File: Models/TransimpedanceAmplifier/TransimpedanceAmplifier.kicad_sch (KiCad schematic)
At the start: 2 parts, among them SW1 SW_SPDT, SW2 SW_SPDT_312

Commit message: Refactoring in progress
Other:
- note added: "Legend for bypass capacitors 0603 case size: 100 nF - 100 V, X7R 220 nF - 50 V, X7R 1 uF - 50 V, X5R 0805 case size: 1 uF - 50 V, X7R 10 uF - 25 V, X5R"
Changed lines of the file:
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@@
 	(generator_version "9.0")
 	(paper "A4")
+	(rectangle
+		(start 226.06 124.46)
+		(end 266.7 157.48)
+		(stroke
+			(width 0)
+			(type default)
+		)
+		(fill
+			(type none)
+		)
+	)
+	(text "Legend for bypass capacitors\n\n0603 case size:\n100 nF - 100 V, X7R\n220 nF - 50 V, X7R\n1 uF - 50 V, X5R\n\n0805 case size:\n1 uF - 50 V, X7R\n10 uF - 25 V, X5R"
+		(exclude_from_sim no)
+		(at 231.902 129.54 0)
+		(effects
+			(font
+				(size 1.27 1.27)
+			)
+			(justify left top)
+		)
+	)
 	(text "TODO: Limit current of bias voltage supply\nto <5 mA to prevent damage to AD8615"
 		(exclude_from_sim no)

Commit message: Save progress
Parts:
- removed SW2: SW_SPDT_312, symbol Switch:SW_SPDT_312
- added J2: Conn_01x03_Pin, symbol Connector:Conn_01x03_Pin
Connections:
- net CPU/ADC_Input: now also J2.2 (Pin_2)
- net TIA_OneStage/Output: now also J2.1 (Pin_1)
- net TIA_TwoStage/Output: now also J2.3 (Pin_3)
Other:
- note added: "Jumper selects which TIA to test Alternatively, connect DAC output directly to pin 2"
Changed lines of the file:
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@@
+		)
+	)
+	(text "Jumper selects which TIA to test\nAlternatively, connect DAC output\ndirectly to pin 2"
+		(exclude_from_sim no)
+		(at 167.132 124.46 0)
+		(effects
+			(font
+				(size 1.27 1.27)
+			)
+			(justify left top)
 		)
 	)
@@
 	(wire
 		(pts
+			(xy 165.1 96.52) (xy 165.1 119.38)
+		)
+		(stroke
+			(width 0)
+			(type default)
+		)
+	)
+	(wire
+		(pts
+			(xy 165.1 121.92) (xy 172.72 121.92)
+		)
+		(stroke
+			(width 0)
+			(type default)
+		)
+	)
+	(wire
+		(pts
 			(xy 40.64 45.72) (xy 104.14 45.72)
 		)
@@
 	(wire
 		(pts
+			(xy 165.1 124.46) (xy 165.1 147.32)
+		)
+		(stroke
+			(width 0)
+			(type default)
+		)
+	)
+	(wire
+		(pts
 			(xy 93.98 124.46) (xy 99.06 124.46)
 		)
@@
 	(wire
 		(pts
-			(xy 144.78 45.72) (xy 170.18 45.72)
-		)
-		(stroke
-			(width 0)
-			(type default)
-		)
-	)
-	(wire
-		(pts
-			(xy 165.1 121.92) (xy 170.18 121.92)
-		)
-		(stroke
-			(width 0)
-			(type default)
-		)
-	)
-	(wire
-		(pts
 			(xy 99.06 96.52) (xy 104.14 96.52)
 		)
@@
 	(wire
 		(pts
+			(xy 172.72 121.92) (xy 172.72 45.72)
+		)
+		(stroke
+			(width 0)
+			(type default)
+		)
+	)
+	(wire
+		(pts
 			(xy 99.06 119.38) (xy 99.06 96.52)
 		)
@@
 	(wire
 		(pts
-			(xy 144.78 96.52) (xy 149.86 96.52)
-		)
-		(stroke
-			(width 0)
-			(type default)
-		)
-	)
-	(wire
-		(pts
-			(xy 149.86 124.46) (xy 154.94 124.46)
-		)
-		(stroke
-			(width 0)
-			(type default)
-		)
-	)
-	(wire
-		(pts
-			(xy 149.86 147.32) (xy 149.86 124.46)
-		)
-		(stroke
-			(width 0)
-			(type default)
-		)
-	)
-	(wire
-		(pts
 			(xy 78.74 121.92) (xy 83.82 121.92)
 		)
@@
 	(wire
 		(pts
-			(xy 149.86 119.38) (xy 154.94 119.38)
+			(xy 144.78 96.52) (xy 165.1 96.52)
+		)
+		(stroke
+			(width 0)
+			(type default)
+		)
+	)
+	(wire
+		(pts
+			(xy 144.78 45.72) (xy 172.72 45.72)
 		)
 		(stroke
@@
 	(wire
 		(pts
-			(xy 144.78 147.32) (xy 149.86 147.32)
-		)
-		(stroke
-			(width 0)
-			(type default)
-		)
-	)
-	(wire
-		(pts
-			(xy 149.86 96.52) (xy 149.86 119.38)
-		)
-		(stroke
-			(width 0)
-			(type default)
-		)
-	)
-	(wire
-		(pts
 			(xy 40.64 121.92) (xy 40.64 45.72)
 		)
@@
 	(wire
 		(pts
+			(xy 144.78 147.32) (xy 165.1 147.32)
+		)
+		(stroke
+			(width 0)
+			(type default)
+		)
+	)
+	(wire
+		(pts
 			(xy 99.06 147.32) (xy 104.14 147.32)
-		)
-		(stroke
-			(width 0)
-			(type default)
-		)
-	)
-	(wire
-		(pts
-			(xy 170.18 121.92) (xy 170.18 45.72)
 		)
 		(stroke
@@
 			)
 			(justify left bottom)
+		)
+	)
+	(symbol
+		(lib_id "Connector:Conn_01x03_Pin")
+		(at 160.02 121.92 0)
+		(unit 1)
+		(exclude_from_sim no)
+		(in_bom yes)
+		(on_board yes)
+		(dnp no)
+		(property "Reference" "J2"
+			(at 157.734 120.396 0)
+			(effects
+				(font
+					(size 1.27 1.27)
+				)
+			)
+		)
+		(property "Value" "Conn_01x03_Pin"
+			(at 151.384 122.936 0)
+			(effects
+				(font
+					(size 1.27 1.27)
+				)
+			)
+		)
+		(property "Footprint" ""
+			(at 160.02 121.92 0)
+			(effects
+				(font
+					(size 1.27 1.27)
+				)
+				(hide yes)
+			)
+		)
+		(property "Datasheet" "~"
+			(at 160.02 121.92 0)
+			(effects
+				(font
+					(size 1.27 1.27)
+				)
+				(hide yes)
+			)
+		)
+		(property "Description" "Generic connector, single row, 01x03, script generated"
+			(at 160.02 121.92 0)
+			(effects
+				(font
+					(size 1.27 1.27)
+				)
+				(hide yes)
+			)
+		)
+		(pin "1"
+		)
+		(pin "2"
+		)
+		(pin "3"
+		)
+		(instances
+			(project ""
+				(path "/ec9f2ae3-e40d-40eb-9760-2b611ee8efd1"
+					(reference "J2")
+					(unit 1)
+				)
+			)
 		)
 	)
@@
 					(unit 1)
 				)
-			)
-		)
-	)
-	(symbol
-		(lib_id "Switch:SW_SPDT_312")
-		(at 160.02 121.92 0)
-		(mirror y)
-		(unit 1)
-		(exclude_from_sim no)
-		(in_bom yes)
-		(on_board yes)
-		(dnp no)
-		(property "Reference" "SW2"
-			(at 160.02 113.03 0)
-			(effects
-				(font
-					(size 1.27 1.27)
-				)
-			)
-		)
-		(property "Value" "SW_SPDT_312"
-			(at 160.02 115.57 0)
-			(effects
-				(font
-					(size 1.27 1.27)
-				)
-			)
-		)
-		(property "Footprint" ""
-			(at 160.02 132.08 0)
-			(effects
-				(font
-					(size 1.27 1.27)
-				)
-				(hide yes)
-			)
-		)
-		(property "Datasheet" "~"
-			(at 160.02 129.54 0)
-			(effects
-				(font
-					(size 1.27 1.27)
-				)
-				(hide yes)
-			)
-		)
-		(property "Description" "Switch, single pole double throw"
-			(at 160.02 121.92 0)
-			(effects
-				(font
-					(size 1.27 1.27)
-				)
-				(hide yes)
-			)
-		)
-		(pin "2"
-		)
-		(pin "1"
-		)
-		(pin "3"
-		)
-		(instances
-			(project ""
-				(path "/ec9f2ae3-e40d-40eb-9760-2b611ee8efd1"
-					(reference "SW2")
-					(unit 1)
-				)

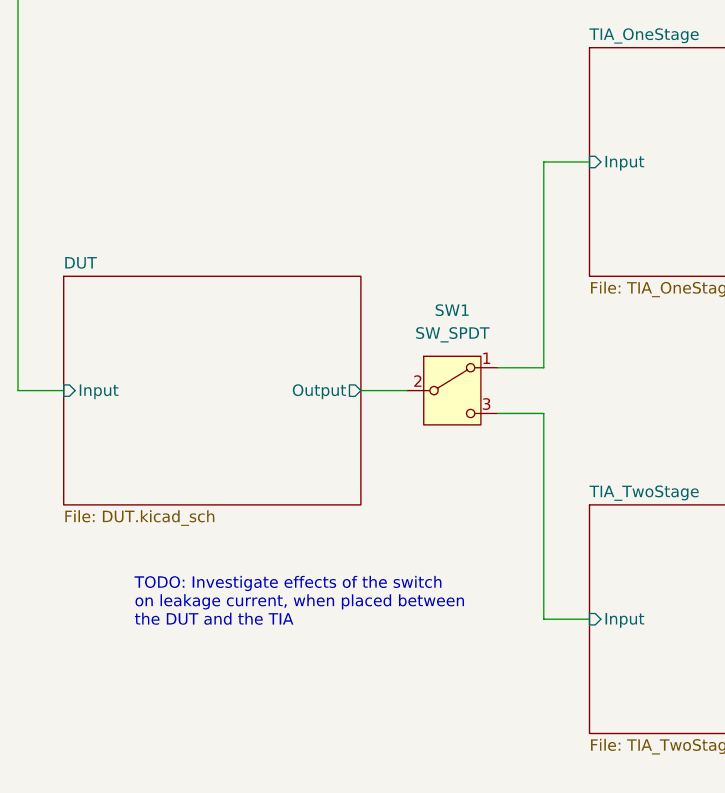
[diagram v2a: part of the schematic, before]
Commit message: Next step is to refactor the power net at each op-amp
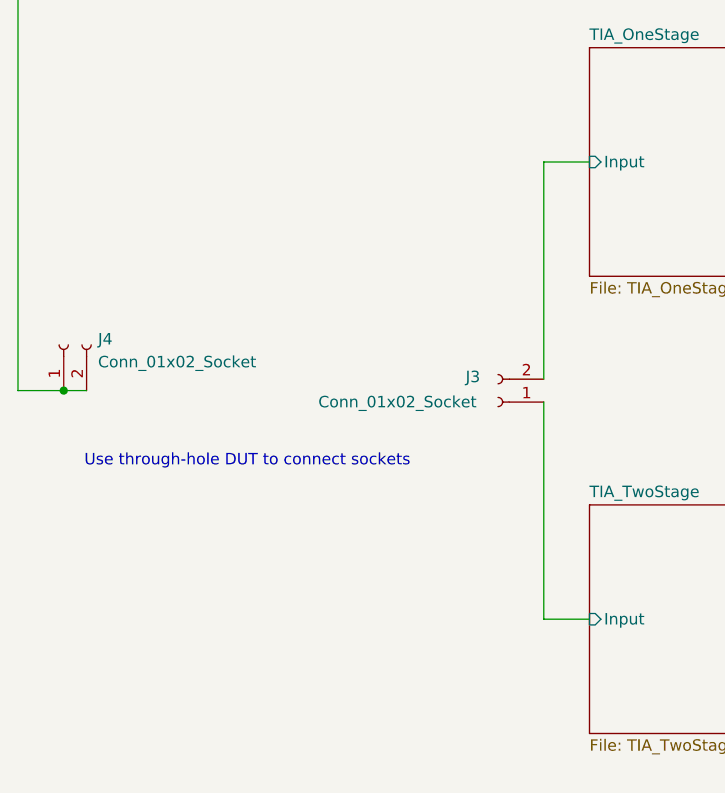
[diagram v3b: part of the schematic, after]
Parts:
- removed SW1: SW_SPDT, symbol Switch:SW_SPDT
- added J3, J4: Conn_01x02_Socket, symbol Connector:Conn_01x02_Socket
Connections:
- net CPU/DAC_Output: now also J4.1 (Pin_1), J4.2 (Pin_2)
- net TIA_OneStage/Input: now also J3.2 (Pin_2)
- net TIA_TwoStage/Input: now also J3.1 (Pin_1)
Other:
- removed sheet DUT
- note added: "Use through-hole DUT to connect sockets"
- note removed: "TODO: Investigate effects of the switch on leakage current, when placed between the DUT and the TIA"
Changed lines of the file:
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@@
-		)
-	)
-	(text "TODO: Investigate effects of the switch\non leakage current, when placed between\nthe DUT and the TIA"
-		(exclude_from_sim no)
-		(at 53.594 142.748 0)
-		(effects
-			(font
-				(size 1.27 1.27)
-			)
-			(justify left top)
 		)
 	)
@@
 		)
 	)
-	(wire
-		(pts
-			(xy 45.72 121.92) (xy 40.64 121.92)
-		)
-		(stroke
-			(width 0)
-			(type default)
-		)
+	(text "Use through-hole DUT to connect sockets"
+		(exclude_from_sim no)
+		(at 48.006 129.032 0)
+		(effects
+			(font
+				(size 1.27 1.27)
+			)
+			(justify left top)
+		)
+	)
+	(junction
+		(at 45.72 121.92)
+		(diameter 0)
+		(color 0 0 0 0)
 	)
 	(wire
@@
 	(wire
 		(pts
-			(xy 93.98 124.46) (xy 99.06 124.46)
-		)
-		(stroke
-			(width 0)
-			(type default)
-		)
-	)
-	(wire
-		(pts
 			(xy 99.06 96.52) (xy 104.14 96.52)
 		)
@@
 	(wire
 		(pts
-			(xy 99.06 119.38) (xy 99.06 96.52)
-		)
-		(stroke
-			(width 0)
-			(type default)
-		)
-	)
-	(wire
-		(pts
-			(xy 78.74 121.92) (xy 83.82 121.92)
+			(xy 99.06 96.52) (xy 99.06 120.65)
+		)
+		(stroke
+			(width 0)
+			(type default)
+		)
+	)
+	(wire
+		(pts
+			(xy 40.64 121.92) (xy 45.72 121.92)
 		)
 		(stroke
@@
 	(wire
 		(pts
-			(xy 99.06 124.46) (xy 99.06 147.32)
-		)
-		(stroke
-			(width 0)
-			(type default)
-		)
-	)
-	(wire
-		(pts
-			(xy 93.98 119.38) (xy 99.06 119.38)
+			(xy 45.72 121.92) (xy 48.26 121.92)
 		)
 		(stroke
@@
 		(pts
 			(xy 144.78 147.32) (xy 165.1 147.32)
+		)
+		(stroke
+			(width 0)
+			(type default)
+		)
+	)
+	(wire
+		(pts
+			(xy 99.06 123.19) (xy 99.06 147.32)
 		)
 		(stroke
@@
 			)
 			(justify left bottom)
+		)
+	)
+	(symbol
+		(lib_id "Connector:Conn_01x02_Socket")
+		(at 93.98 123.19 180)
+		(unit 1)
+		(exclude_from_sim no)
+		(in_bom yes)
+		(on_board yes)
+		(dnp no)
+		(property "Reference" "J3"
+			(at 91.186 120.396 0)
+			(effects
+				(font
+					(size 1.27 1.27)
+				)
+			)
+		)
+		(property "Value" "Conn_01x02_Socket"
+			(at 82.804 123.19 0)
+			(effects
+				(font
+					(size 1.27 1.27)
+				)
+			)
+		)
+		(property "Footprint" ""
+			(at 93.98 123.19 0)
+			(effects
+				(font
+					(size 1.27 1.27)
+				)
+				(hide yes)
+			)
+		)
+		(property "Datasheet" "~"
+			(at 93.98 123.19 0)
+			(effects
+				(font
+					(size 1.27 1.27)
+				)
+				(hide yes)
+			)
+		)
+		(property "Description" "Generic connector, single row, 01x02, script generated"
+			(at 93.98 123.19 0)
+			(effects
+				(font
+					(size 1.27 1.27)
+				)
+				(hide yes)
+			)
+		)
+		(pin "1"
+		)
+		(pin "2"
+		)
+		(instances
+			(project ""
+				(path "/ec9f2ae3-e40d-40eb-9760-2b611ee8efd1"
+					(reference "J3")
+					(unit 1)
+				)
+			)
 		)
 	)
@@
 	)
 	(symbol
-		(lib_id "Switch:SW_SPDT")
-		(at 88.9 121.92 0)
+		(lib_id "Connector:Conn_01x02_Socket")
+		(at 45.72 116.84 90)
 		(unit 1)
 		(exclude_from_sim no)
@@
 		(dnp no)
 		(fields_autoplaced yes)
-		(property "Reference" "SW1"
-			(at 88.9 113.03 0)
-			(effects
-				(font
-					(size 1.27 1.27)
-				)
-			)
-		)
-		(property "Value" "SW_SPDT"
-			(at 88.9 115.57 0)
-			(effects
-				(font
-					(size 1.27 1.27)
-				)
+		(property "Reference" "J4"
+			(at 49.53 116.2049 90)
+			(effects
+				(font
+					(size 1.27 1.27)
+				)
+				(justify right)
+			)
+		)
+		(property "Value" "Conn_01x02_Socket"
+			(at 49.53 118.7449 90)
+			(effects
+				(font
+					(size 1.27 1.27)
+				)
+				(justify right)
 			)
 		)
 		(property "Footprint" ""
-			(at 88.9 121.92 0)
+			(at 45.72 116.84 0)
 			(effects
 				(font
@@
 		)
 		(property "Datasheet" "~"
-			(at 88.9 129.54 0)
-			(effects
-				(font
-					(size 1.27 1.27)
-				)
-				(hide yes)
-			)
-		)
-		(property "Description" "Switch, single pole double throw"
-			(at 88.9 121.92 0)
-			(effects
-				(font
-					(size 1.27 1.27)
-				)
-				(hide yes)
-			)
-		)
-		(pin "3"
+			(at 45.72 116.84 0)
+			(effects
+				(font
+					(size 1.27 1.27)
+				)
+				(hide yes)
+			)
+		)
+		(property "Description" "Generic connector, single row, 01x02, script generated"
+			(at 45.72 116.84 0)
+			(effects
+				(font
+					(size 1.27 1.27)
+				)
+				(hide yes)
+			)
+		)
+		(pin "1"
 		)
 		(pin "2"
-		)
-		(pin "1"
 		)
 		(instances
 			(project ""
 				(path "/ec9f2ae3-e40d-40eb-9760-2b611ee8efd1"
-					(reference "SW1")
+					(reference "J4")
 					(unit 1)
 				)
@@
 				)
 			)
-		)
-	)
-	(sheet
-		(at 45.72 109.22)
-		(size 33.02 25.4)
-		(exclude_from_sim no)
-		(in_bom yes)
-		(on_board yes)
-		(dnp no)
-		(fields_autoplaced yes)
-		(stroke
-			(width 0.1524)
-			(type solid)
-		)
-		(fill
-			(color 0 0 0 0.0000)
-		)
-		(property "Sheetname" "DUT"
-			(at 45.72 108.5084 0)
-			(effects
-				(font
-					(size 1.27 1.27)
-				)
-				(justify left bottom)
-			)
-		)
-		(property "Sheetfile" "DUT.kicad_sch"
-			(at 45.72 135.2046 0)
-			(effects
-				(font
-					(size 1.27 1.27)
-				)
-				(justify left top)
-			)
-		)
-		(pin "Input" input
-			(at 45.72 121.92 180)
-			(effects
-				(font
-					(size 1.27 1.27)
-				)
-				(justify left)
-			)
-		)
-		(pin "Output" output
-			(at 78.74 121.92 0)
-			(effects
-				(font
-					(size 1.27 1.27)
-				)
-				(justify right)
-			)
-		)
-		(instances
-			(project "TransimpedanceAmplifier"
-				(path "/ec9f2ae3-e40d-40eb-9760-2b611ee8efd1"
-					(page "5")
-				)
-			)

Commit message: Save progress
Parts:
- J2, J3, J4: Purchase Link (none) -> https://www.digikey.com/en/products/detail/sullins-connecto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
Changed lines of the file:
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@@
+			)
+		)
+		(property "Purchase Link" "https://www.digikey.com/en/products/detail/sullins-connector-solutions/PPPC021LFBN-RC/810174"
+			(at 93.98 123.19 0)
+			(effects
+				(font
+					(size 1.27 1.27)
+				)
+				(hide yes)
 			)
 		)
@@
 		)
 		(property "Description" "Generic connector, single row, 01x03, script generated"
+			(at 160.02 121.92 0)
+			(effects
+				(font
+					(size 1.27 1.27)
+				)
+				(hide yes)
+			)
+		)
+		(property "Purchase Link" "https://www.digikey.com/en/products/detail/sullins-connector-solutions/QPC02SXGN-RC/2618262"
 			(at 160.02 121.92 0)
 			(effects
@@
 			(effects
 				(font
+					(size 1.27 1.27)
+				)
+				(hide yes)
+			)
+		)
+		(property "Purchase Link" "https://www.digikey.com/en/products/detail/sullins-connector-solutions/PPPC021LFBN-RC/810174"
+			(at 45.72 116.84 90)
+			(effects
+				(font

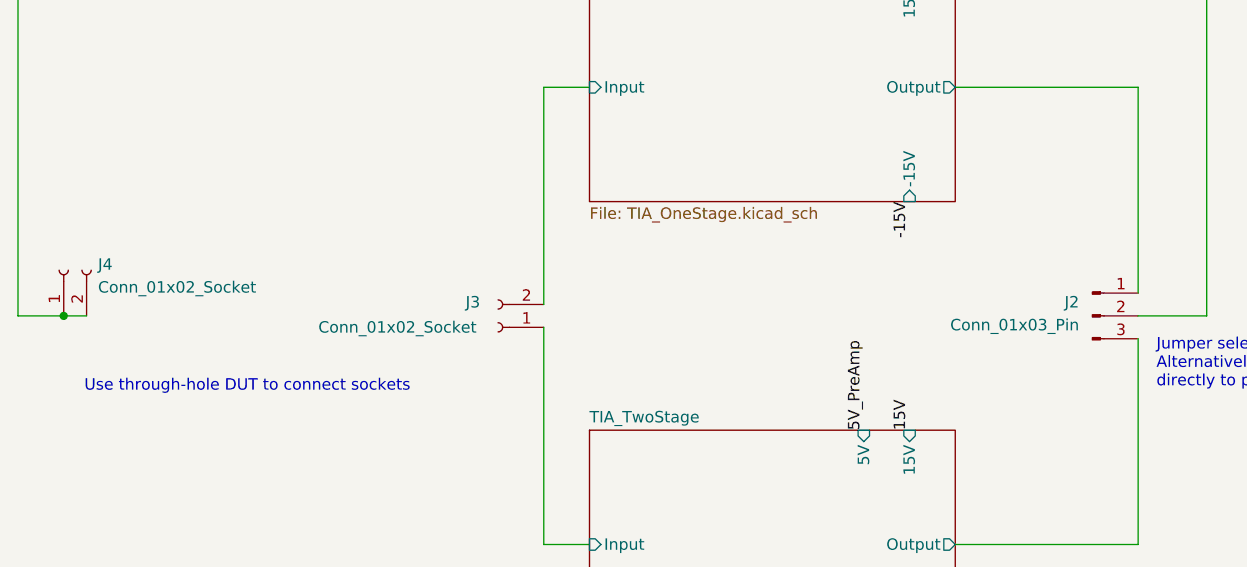
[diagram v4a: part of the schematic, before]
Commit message: Overhauled all of the annotations
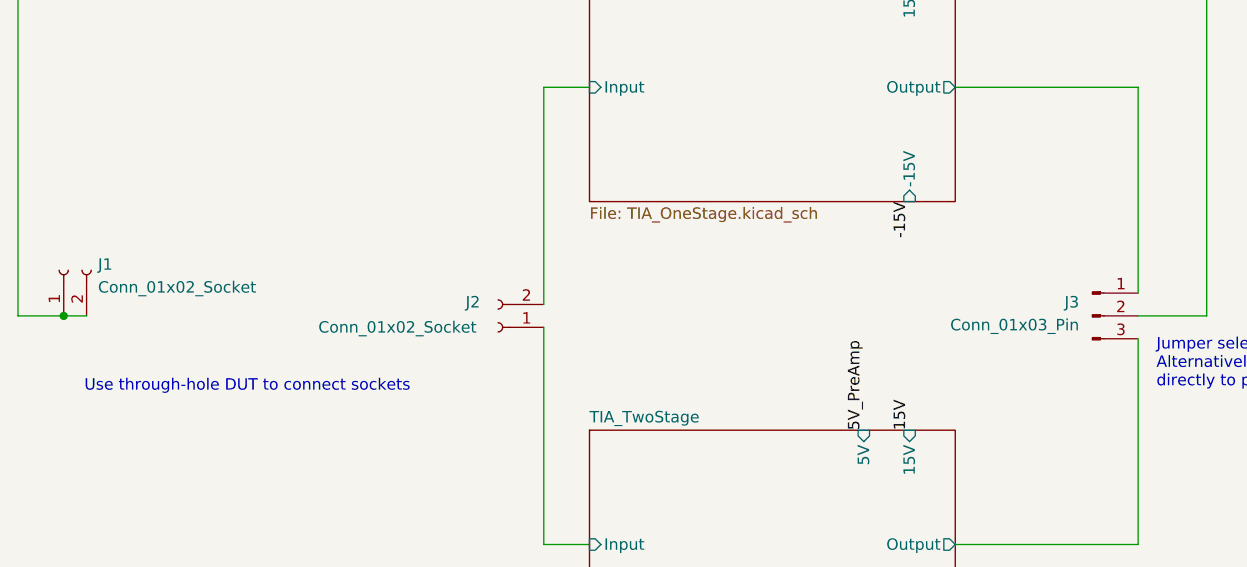
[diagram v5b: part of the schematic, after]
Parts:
- renumbered J4 to J1, J3 to J2, J2 to J3
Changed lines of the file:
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@@
 		(on_board yes)
 		(dnp no)
-		(property "Reference" "J3"
+		(property "Reference" "J2"
 			(at 91.186 120.396 0)
 			(effects
@@
 			(project ""
 				(path "/ec9f2ae3-e40d-40eb-9760-2b611ee8efd1"
-					(reference "J3")
+					(reference "J2")
 					(unit 1)
 				)
@@
 		(on_board yes)
 		(dnp no)
-		(property "Reference" "J2"
+		(property "Reference" "J3"
 			(at 157.734 120.396 0)
 			(effects
@@
 			(project ""
 				(path "/ec9f2ae3-e40d-40eb-9760-2b611ee8efd1"
-					(reference "J2")
+					(reference "J3")
 					(unit 1)
 				)
@@
 		(dnp no)
 		(fields_autoplaced yes)
-		(property "Reference" "J4"
+		(property "Reference" "J1"
 			(at 49.53 116.2049 90)
 			(effects
@@
 			(project ""
 				(path "/ec9f2ae3-e40d-40eb-9760-2b611ee8efd1"
-					(reference "J4")
+					(reference "J1")
 					(unit 1)
 				)
